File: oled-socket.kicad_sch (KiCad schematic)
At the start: 16 parts, among them IC17 TPS6734IDR, J5 3-2328724-1

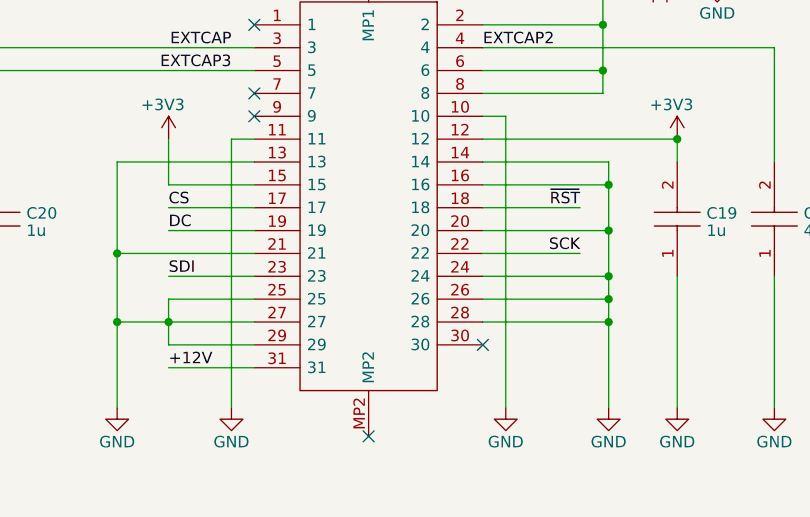
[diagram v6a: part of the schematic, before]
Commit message: add debug througholes for wiring up debug lines
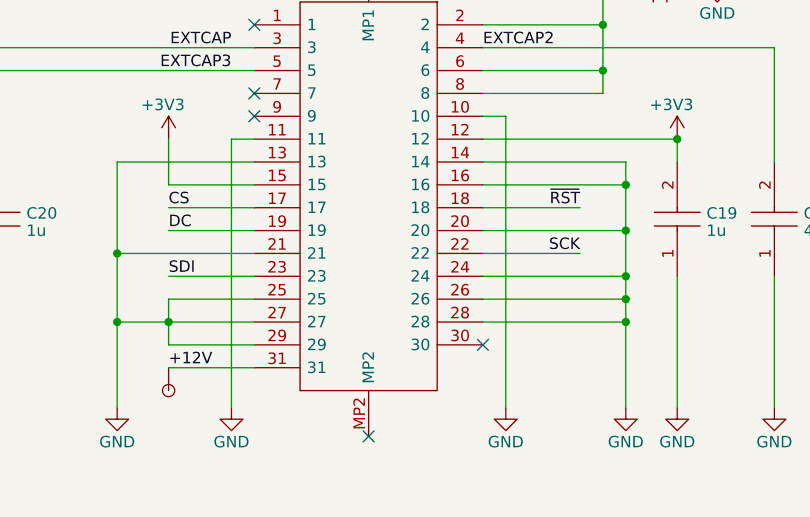
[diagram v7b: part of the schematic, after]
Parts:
- added DBG1: ~, Oro Footprints:DebugPin, symbol Oro:DebugPin
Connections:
- net +12V: now also DBG1.1
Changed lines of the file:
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@@
   (junction (at 223.52 125.73) (diameter 0) (color 0 0 0 0)
   )
-  (junction (at 113.03 102.87) (diameter 0) (color 0 0 0 0)
+  (junction (at 114.935 102.87) (diameter 0) (color 0 0 0 0)
   )
   (junction (at 261.62 104.14) (diameter 0) (color 0 0 0 0)
@@
   (junction (at 236.22 114.3) (diameter 0) (color 0 0 0 0)
   )
-  (junction (at 113.03 115.57) (diameter 0) (color 0 0 0 0)
-  )
-  (junction (at 113.03 118.11) (diameter 0) (color 0 0 0 0)
+  (junction (at 114.935 115.57) (diameter 0) (color 0 0 0 0)
+  )
+  (junction (at 114.935 118.11) (diameter 0) (color 0 0 0 0)
   )
   (junction (at 112.395 80.01) (diameter 0) (color 0 0 0 0)
   )
-  (junction (at 113.03 113.03) (diameter 0) (color 0 0 0 0)
-  )
-  (junction (at 113.03 107.95) (diameter 0) (color 0 0 0 0)
+  (junction (at 114.935 113.03) (diameter 0) (color 0 0 0 0)
+  )
+  (junction (at 114.935 107.95) (diameter 0) (color 0 0 0 0)
   )
   (junction (at 236.22 119.38) (diameter 0) (color 0 0 0 0)
@@
     (stroke (width 0) (type default))
   )
-  (wire (pts (xy 113.03 118.11) (xy 113.03 127.635))
+  (wire (pts (xy 114.935 118.11) (xy 114.935 127.635))
     (stroke (width 0) (type default))
   )
@@
     (stroke (width 0) (type default))
   )
-  (wire (pts (xy 113.03 100.33) (xy 113.03 102.87))
+  (wire (pts (xy 114.935 100.33) (xy 114.935 102.87))
     (stroke (width 0) (type default))
   )
@@
     (stroke (width 0) (type default))
   )
-  (wire (pts (xy 99.06 102.87) (xy 113.03 102.87))
+  (wire (pts (xy 99.06 102.87) (xy 114.935 102.87))
     (stroke (width 0) (type default))
   )
@@
     (stroke (width 0) (type default))
   )
-  (wire (pts (xy 99.06 100.33) (xy 113.03 100.33))
+  (wire (pts (xy 99.06 100.33) (xy 114.935 100.33))
     (stroke (width 0) (type default))
   )
@@
     (stroke (width 0) (type default))
   )
-  (wire (pts (xy 99.06 115.57) (xy 113.03 115.57))
+  (wire (pts (xy 99.06 115.57) (xy 114.935 115.57))
     (stroke (width 0) (type default))
   )
@@
     (stroke (width 0) (type default))
   )
-  (wire (pts (xy 99.06 118.11) (xy 113.03 118.11))
-    (stroke (width 0) (type default))
-  )
-  (wire (pts (xy 99.06 113.03) (xy 113.03 113.03))
+  (wire (pts (xy 99.06 118.11) (xy 114.935 118.11))
+    (stroke (width 0) (type default))
+  )
+  (wire (pts (xy 99.06 113.03) (xy 114.935 113.03))
     (stroke (width 0) (type default))
   )
@@
     (stroke (width 0) (type default))
   )
-  (wire (pts (xy 113.03 102.87) (xy 113.03 107.95))
+  (wire (pts (xy 114.935 102.87) (xy 114.935 107.95))
     (stroke (width 0) (type default))
   )
@@
     (stroke (width 0) (type default))
   )
-  (wire (pts (xy 99.06 107.95) (xy 113.03 107.95))
+  (wire (pts (xy 99.06 107.95) (xy 114.935 107.95))
     (stroke (width 0) (type default))
   )
@@
     (stroke (width 0) (type dot))
   )
-  (wire (pts (xy 113.03 107.95) (xy 113.03 113.03))
+  (wire (pts (xy 114.935 107.95) (xy 114.935 113.03))
     (stroke (width 0) (type default))
   )
@@
     (stroke (width 0) (type default))
   )
-  (wire (pts (xy 113.03 115.57) (xy 113.03 118.11))
+  (wire (pts (xy 114.935 115.57) (xy 114.935 118.11))
     (stroke (width 0) (type default))
   )
@@
     (stroke (width 0) (type default))
   )
-  (wire (pts (xy 113.03 113.03) (xy 113.03 115.57))
+  (wire (pts (xy 114.935 113.03) (xy 114.935 115.57))
     (stroke (width 0) (type default))
   )
@@
     )
   )
+  (symbol (lib_id "Oro:DebugPin") (at 64.135 123.19 270) (unit 1)
+    (in_bom no) (on_board yes) (dnp no)
+    (property "Reference" "DBG1" (at 66.675 127.635 90)
+      (effects (font (size 1.27 1.27)) (justify right) hide)
+    )
+    (property "Value" "~" (at 64.135 123.19 0)
+      (effects (font (size 1.27 1.27)) hide)
+    )
+    (property "Footprint" "Oro Footprints:DebugPin" (at 66.675 124.46 0)
+      (effects (font (size 1.27 1.27)) hide)
+    )
+    (property "Datasheet" "" (at 64.135 123.19 0)
+      (effects (font (size 1.27 1.27)) hide)
+    )
+    (property "Sim.Enable" "0" (at 66.675 137.16 0)
+      (effects (font (size 1.27 1.27)) hide)
+    )
+    (pin "1")
+    (instances
+      (project "OroLink"
+        (path "/e89dcd22-1250-4a5b-b778-1c95a0dd623d/f955395e-bf1a-4ef3-9cfe-ec9d49f66988"
+          (reference "DBG1") (unit 1)
+        )
+        (path "/e89dcd22-1250-4a5b-b778-1c95a0dd623d/dd173832-34f8-47c0-be66-f527d6e2d134"
+          (reference "DBG8") (unit 1)
+        )
+        (path "/e89dcd22-1250-4a5b-b778-1c95a0dd623d/1b3eede1-74b0-4c0b-b4f1-7ec1bfc1f54f"
+          (reference "DBG38") (unit 1)
+        )
+      )
+    )
+  )
   (symbol (lib_id "power:GND") (at 120.65 127.635 0) (unit 1)
     (in_bom yes) (on_board yes) (dnp no)
@@
     )
   )
-  (symbol (lib_id "power:GND") (at 113.03 127.635 0) (mirror y) (unit 1)
+  (symbol (lib_id "power:GND") (at 114.935 127.635 0) (mirror y) (unit 1)
     (in_bom yes) (on_board yes) (dnp no)
-    (property "Reference" "#PWR026" (at 113.03 133.985 0)
-      (effects (font (size 1.27 1.27)) hide)
-    )
-    (property "Value" "GND" (at 113.03 131.445 0)
-      (effects (font (size 1.27 1.27)))
-    )
-    (property "Footprint" "" (at 113.03 127.635 0)
-      (effects (font (size 1.27 1.27)) hide)
-    )
-    (property "Datasheet" "" (at 113.03 127.635 0)
-      (effects (font (size 1.27 1.27)) hide)
-    )
+    (property "Reference" "#PWR026" (at 114.935 133.985 0)
+      (effects (font (size 1.27 1.27)) hide)
+    )
+    (property "Value" "GND" (at 114.935 131.445 0)
+      (effects (font (size 1.27 1.27)))
+    )
+    (property "Footprint" "" (at 114.935 127.635 0)
+      (effects (font (size 1.27 1.27)) hide)
+    )
+    (property "Datasheet" "" (at 114.935 127.635 0)
+      (effects (font (size 1.27 1.27)) hide)
+    )
